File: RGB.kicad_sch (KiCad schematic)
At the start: 2 parts

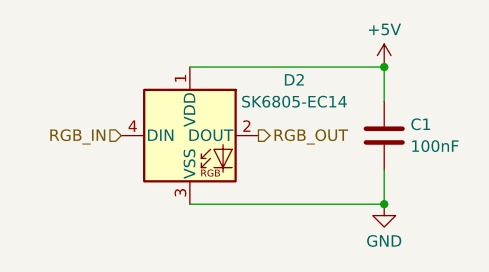
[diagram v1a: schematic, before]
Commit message: Add power / invader logo light
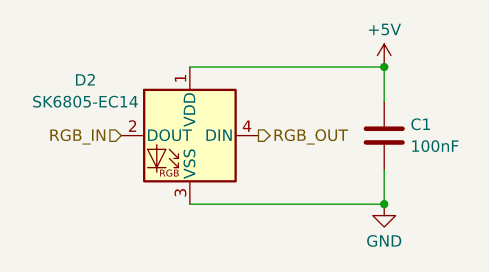
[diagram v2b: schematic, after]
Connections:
- net RGB_IN: now also D2.2 (DOUT); no longer D2.4 (DIN)
- net RGB_OUT: now also D2.4 (DIN); no longer D2.2 (DOUT)
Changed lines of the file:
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@@
+					(unit 1)
+				)
+				(path "/279815f6-a512-43c8-bc8d-a03c0593ab83/c2f10722-089c-46ea-ab0f-0e2e905d0c64"
+					(reference "C89")
 					(unit 1)
 				)
@@
 					(unit 1)
 				)
+				(path "/279815f6-a512-43c8-bc8d-a03c0593ab83/c2f10722-089c-46ea-ab0f-0e2e905d0c64"
+					(reference "#PWR0191")
+					(unit 1)
+				)
 				(path "/279815f6-a512-43c8-bc8d-a03c0593ab83/d08ae5e3-6b99-4313-96e0-b4a8d5e149a0"
 					(reference "#PWR0122")
@@
 					(unit 1)
 				)
+				(path "/279815f6-a512-43c8-bc8d-a03c0593ab83/c2f10722-089c-46ea-ab0f-0e2e905d0c64"
+					(reference "#PWR0190")
+					(unit 1)
+				)
 				(path "/279815f6-a512-43c8-bc8d-a03c0593ab83/d08ae5e3-6b99-4313-96e0-b4a8d5e149a0"
 					(reference "#PWR0121")
@@
 		(lib_id "DecentUSB_Library:SK6812MINI")
 		(at 140.97 95.25 0)
+		(mirror y)
 		(unit 1)
 		(exclude_from_sim no)
@@
 		(on_board yes)
 		(dnp no)
-		(fields_autoplaced yes)
 		(property "Reference" "D2"
-			(at 152.5777 89.105 0)
+			(at 129.3623 89.105 0)
 			(effects
 				(font
@@
 		)
 		(property "Value" "SK6805-EC14"
-			(at 152.5777 91.5293 0)
+			(at 129.3623 91.5293 0)
 			(effects
 				(font
@@
 		)
 		(property "Footprint" "easyeda2kicad:LED-SMD_4P-L1.4-W1.4-TL"
-			(at 142.24 102.87 0)
+			(at 139.7 102.87 0)
 			(effects
 				(font
@@
 		)
 		(property "Datasheet" "https://jlcpcb.com/api/file/downloadByFileSystemAccessId/8589042051015462912"
-			(at 143.51 104.775 0)
+			(at 138.43 104.775 0)
 			(effects
 				(font
@@
 					(unit 1)
 				)
+				(path "/279815f6-a512-43c8-bc8d-a03c0593ab83/c2f10722-089c-46ea-ab0f-0e2e905d0c64"
+					(reference "D73")
+					(unit 1)
+				)
